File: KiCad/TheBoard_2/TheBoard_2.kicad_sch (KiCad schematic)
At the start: 9 parts, among them J1 Conn_01x03_Female, J2 Conn_01x03_Female, J3 Conn_01x16_Female, J4 Conn_01x32_Male, J5 Conn_01x16_Female

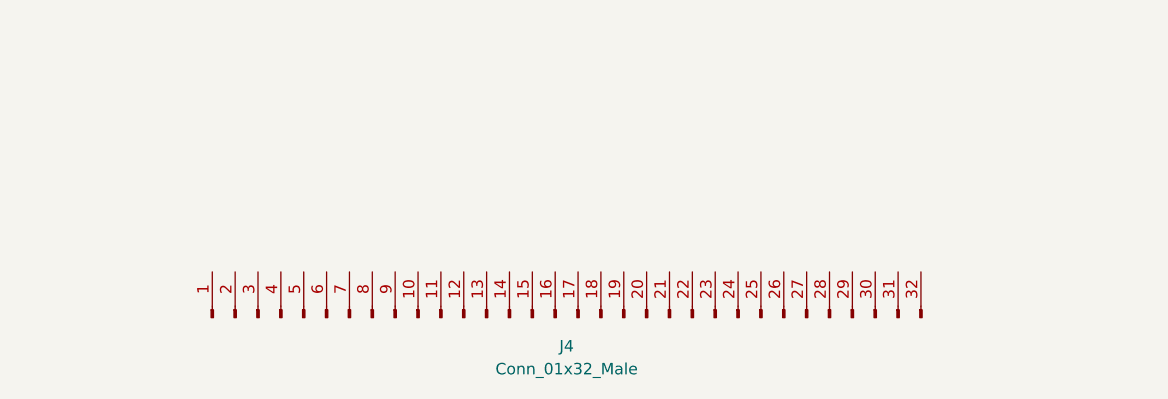
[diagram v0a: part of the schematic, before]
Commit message: Adding ground to output pins
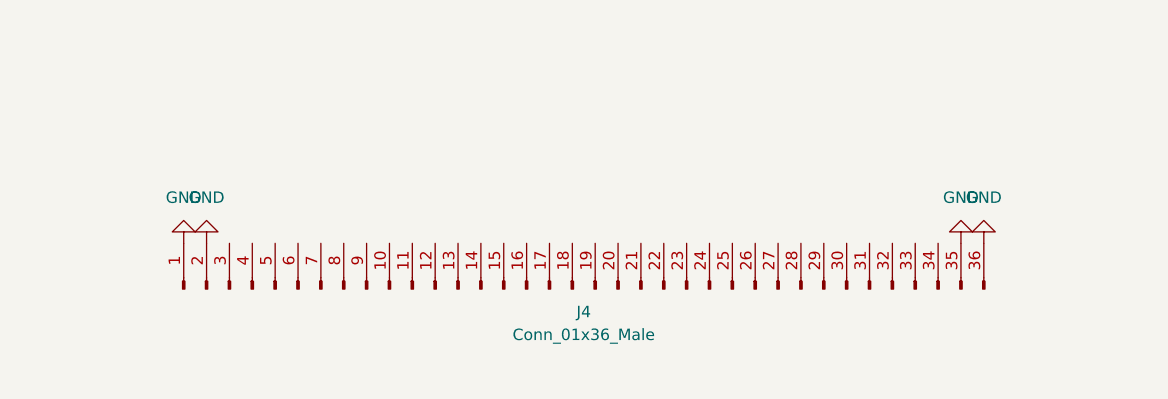
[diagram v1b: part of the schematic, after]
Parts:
- removed J4: Conn_01x32_Male, Connector_PinHeader_2.54mm:PinHeader_1x32_P2.54mm_Horizontal, symbol Connector:Conn_01x32_Male
- added J4: Conn_01x36_Male, Connector_PinHeader_2.54mm:PinHeader_2x18_P2.54mm_Horizontal, symbol Connector:Conn_01x36_Male
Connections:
- net GND: now also J4.1 (Pin_1), J4.2 (Pin_2), J4.35 (Pin_35), J4.36 (Pin_36)
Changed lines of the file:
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@@
     (pin "9")
   )
+  (symbol (lib_id "power:GND") (at 104.14 142.24 180) (unit 1)
+    (in_bom yes) (on_board yes) (fields_autoplaced)
+    (property "Reference" "#PWR0109" (id 0) (at 104.14 135.89 0)
+      (effects (font (size 1.27 1.27)) hide)
+    )
+    (property "Value" "GND" (id 1) (at 104.14 137.16 0))
+    (property "Footprint" "" (id 2) (at 104.14 142.24 0)
+      (effects (font (size 1.27 1.27)) hide)
+    )
+    (property "Datasheet" "" (id 3) (at 104.14 142.24 0)
+      (effects (font (size 1.27 1.27)) hide)
+    )
+    (pin "1")
+  )
   (symbol (lib_id "Mechanical:MountingHole") (at 36.195 30.48 0) (unit 1)
     (in_bom yes) (on_board yes) (fields_autoplaced)
@@
     )
   )
-  (symbol (lib_id "Mechanical:MountingHole") (at 36.195 20.32 0) (unit 1)
-    (in_bom yes) (on_board yes) (fields_autoplaced)
-    (property "Reference" "H2" (id 0) (at 38.735 19.0499 0)
-      (effects (font (size 1.27 1.27)) (justify left))
-    )
-    (property "Value" "MountingHole" (id 1) (at 38.735 21.5899 0)
-      (effects (font (size 1.27 1.27)) (justify left))
-    )
-    (property "Footprint" "MountingHole:MountingHole_3mm" (id 2) (at 36.195 20.32 0)
-      (effects (font (size 1.27 1.27)) hide)
-    )
-    (property "Datasheet" "~" (id 3) (at 36.195 20.32 0)
-      (effects (font (size 1.27 1.27)) hide)
-    )
-  )
-  (symbol (lib_id "Connector:Conn_01x32_Male") (at 145.415 150.495 90) (unit 1)
-    (in_bom yes) (on_board yes) (fields_autoplaced)
-    (property "Reference" "J4" (id 0) (at 146.685 153.67 90))
-    (property "Value" "Conn_01x32_Male" (id 1) (at 146.685 156.21 90))
-    (property "Footprint" "Connector_PinHeader_2.54mm:PinHeader_1x32_P2.54mm_Horizontal" (id 2) (at 145.415 150.495 0)
-      (effects (font (size 1.27 1.27)) hide)
-    )
-    (property "Datasheet" "~" (id 3) (at 145.415 150.495 0)
+  (symbol (lib_id "Connector:Conn_01x36_Male") (at 147.32 147.32 90) (unit 1)
+    (in_bom yes) (on_board yes) (fields_autoplaced)
+    (property "Reference" "J4" (id 0) (at 148.59 149.86 90))
+    (property "Value" "Conn_01x36_Male" (id 1) (at 148.59 152.4 90))
+    (property "Footprint" "Connector_PinHeader_2.54mm:PinHeader_2x18_P2.54mm_Horizontal" (id 2) (at 147.32 147.32 0)
+      (effects (font (size 1.27 1.27)) hide)
+    )
+    (property "Datasheet" "~" (id 3) (at 147.32 147.32 0)
       (effects (font (size 1.27 1.27)) hide)
     )
@@
     (pin "31")
     (pin "32")
+    (pin "33")
+    (pin "34")
+    (pin "35")
+    (pin "36")
     (pin "4")
     (pin "5")
@@
     (pin "8")
     (pin "9")
+  )
+  (symbol (lib_id "power:GND") (at 106.68 142.24 180) (unit 1)
+    (in_bom yes) (on_board yes) (fields_autoplaced)
+    (property "Reference" "#PWR0108" (id 0) (at 106.68 135.89 0)
+      (effects (font (size 1.27 1.27)) hide)
+    )
+    (property "Value" "GND" (id 1) (at 106.68 137.16 0))
+    (property "Footprint" "" (id 2) (at 106.68 142.24 0)
+      (effects (font (size 1.27 1.27)) hide)
+    )
+    (property "Datasheet" "" (id 3) (at 106.68 142.24 0)
+      (effects (font (size 1.27 1.27)) hide)
+    )
+    (pin "1")
+  )
+  (symbol (lib_id "Mechanical:MountingHole") (at 36.195 20.32 0) (unit 1)
+    (in_bom yes) (on_board yes) (fields_autoplaced)
+    (property "Reference" "H2" (id 0) (at 38.735 19.0499 0)
+      (effects (font (size 1.27 1.27)) (justify left))
+    )
+    (property "Value" "MountingHole" (id 1) (at 38.735 21.5899 0)
+      (effects (font (size 1.27 1.27)) (justify left))
+    )
+    (property "Footprint" "MountingHole:MountingHole_3mm" (id 2) (at 36.195 20.32 0)
+      (effects (font (size 1.27 1.27)) hide)
+    )
+    (property "Datasheet" "~" (id 3) (at 36.195 20.32 0)
+      (effects (font (size 1.27 1.27)) hide)
+    )
   )
   (symbol (lib_id "Connector:Conn_01x16_Female") (at 233.045 93.98 180) (unit 1)
@@
     (pin "9")
   )
+  (symbol (lib_id "power:GND") (at 193.04 142.24 180) (unit 1)
+    (in_bom yes) (on_board yes) (fields_autoplaced)
+    (property "Reference" "#PWR0107" (id 0) (at 193.04 135.89 0)
+      (effects (font (size 1.27 1.27)) hide)
+    )
+    (property "Value" "GND" (id 1) (at 193.04 137.16 0))
+    (property "Footprint" "" (id 2) (at 193.04 142.24 0)
+      (effects (font (size 1.27 1.27)) hide)
+    )
+    (property "Datasheet" "" (id 3) (at 193.04 142.24 0)
+      (effects (font (size 1.27 1.27)) hide)
+    )
+    (pin "1")
+  )
   (symbol (lib_id "power:GND") (at 38.735 46.99 90) (unit 1)
     (in_bom yes) (on_board yes) (fields_autoplaced)
@@
       (effects (font (size 1.27 1.27)) hide)
     )
+  )
+  (symbol (lib_id "power:GND") (at 190.5 142.24 180) (unit 1)
+    (in_bom yes) (on_board yes) (fields_autoplaced)
+    (property "Reference" "#PWR0110" (id 0) (at 190.5 135.89 0)
+      (effects (font (size 1.27 1.27)) hide)
+    )
+    (property "Value" "GND" (id 1) (at 190.5 137.16 0))
+    (property "Footprint" "" (id 2) (at 190.5 142.24 0)
+      (effects (font (size 1.27 1.27)) hide)
+    )
+    (property "Datasheet" "" (id 3) (at 190.5 142.24 0)
+      (effects (font (size 1.27 1.27)) hide)
+    )
+    (pin "1")
   )
   (symbol (lib_id "power:+5V") (at 38.735 40.005 270) (unit 1)
@@
       (reference "#PWR0106") (unit 1) (value "+5V") (footprint "")
     )
+    (path "/97874707-852c-4f97-b566-d5092c38fab4"
+      (reference "#PWR0107") (unit 1) (value "GND") (footprint "")
+    )
+    (path "/71a5fcca-2c92-4092-bc45-cdfd87fb70bf"
+      (reference "#PWR0108") (unit 1) (value "GND") (footprint "")
+    )
+    (path "/405b8a8b-22d1-47f5-a0bf-927117cf4560"
+      (reference "#PWR0109") (unit 1) (value "GND") (footprint "")
+    )
+    (path "/f1f5bd8f-cb69-40b6-8cd1-2d77afe2a46a"
+      (reference "#PWR0110") (unit 1) (value "GND") (footprint "")
+    )
     (path "/ebb6476c-0275-4763-a9ea-9c05ccdd35fd"
       (reference "H1") (unit 1) (value "MountingHole") (footprint "MountingHole:MountingHole_3mm")
@@
       (reference "J3") (unit 1) (value "Conn_01x16_Female") (footprint "Connector_PinHeader_2.54mm:PinHeader_1x16_P2.54mm_Vertical")
     )
-    (path "/7ea8b26d-d906-4bd8-95c7-418a065c7cd3"
-      (reference "J4") (unit 1) (value "Conn_01x32_Male") (footprint "Connector_PinHeader_2.54mm:PinHeader_1x32_P2.54mm_Horizontal")
+    (path "/6fa6f00b-82f4-4079-87ff-19d2eeb80891"
+      (reference "J4") (unit 1) (value "Conn_01x36_Male") (footprint "Connector_PinHeader_2.54mm:PinHeader_2x18_P2.54mm_Horizontal")
     )
     (path "/8e6013b4-e104-46a8-b12e-cbcbf0a129da"

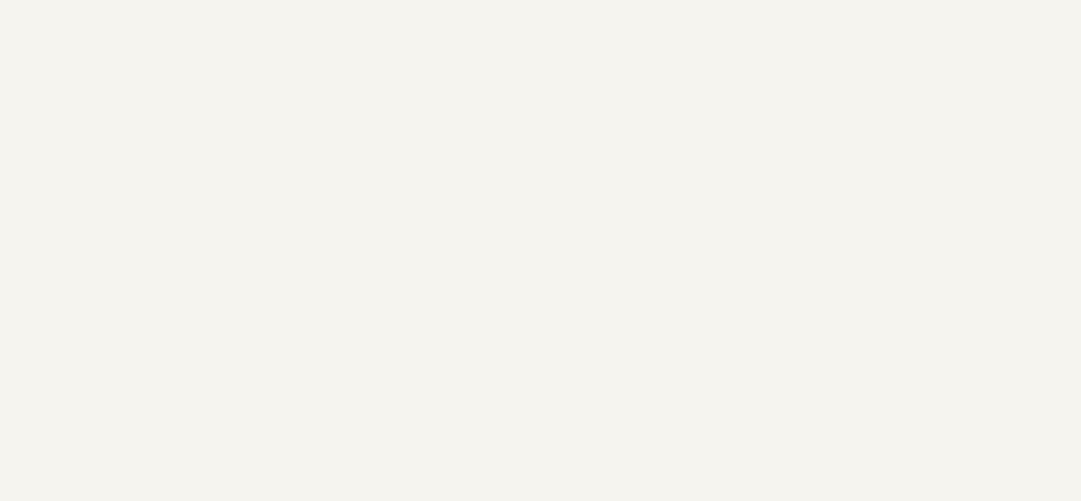
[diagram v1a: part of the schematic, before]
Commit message: Adding -5V circuit
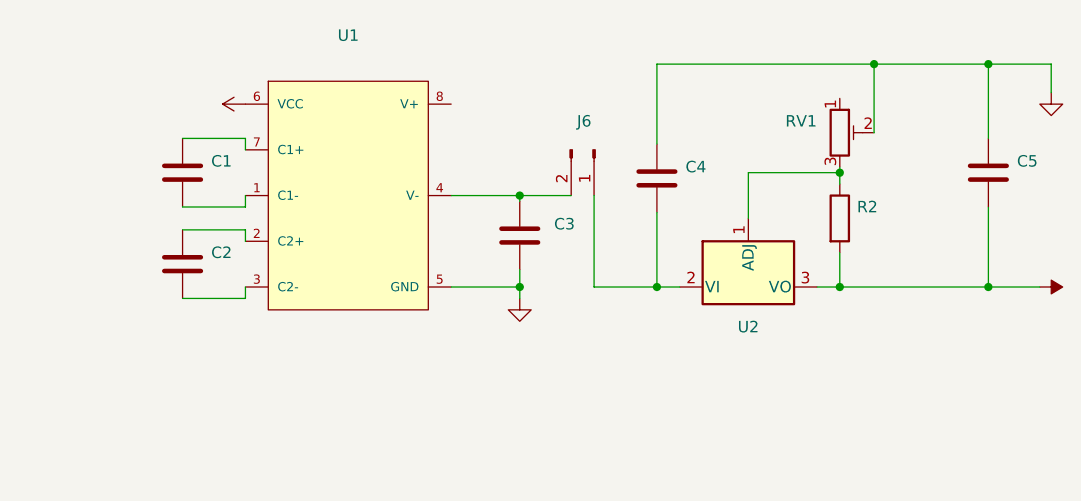
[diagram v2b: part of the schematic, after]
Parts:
- added C1, C2, C3, C4, C5: (no value), symbol Device:C
- added J6: (no value), symbol Connector:Conn_01x02_Male
- added R2: (no value), symbol Device:R
- added RV1: (no value), symbol Device:R_Potentiometer_Trim
- added U1: (no value), symbol eec:MAX680CSA+T
- added U2: (no value), symbol Regulator_Linear:LM337_TO220
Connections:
- net +5V: now also U1.6 (VCC)
- net GND: now also C3.2, C4.1, C5.1, RV1.2, U1.5 (GND)
- new net: R2.1, RV1.3, U2.1 (ADJ)
- new net: C4.2, J6.1 (Pin_1), U2.2 (VI)
- new net: C1.2, U1.1 (C1-)
- new net: C2.1, U1.2 (C2+)
- new net: C2.2, U1.3 (C2-)
- new net: C3.1, J6.2 (Pin_2), U1.4 (V-)
- new net: C1.1, U1.7 (C1+)
- new net -5V: C5.2, R2.2, U2.3 (VO)

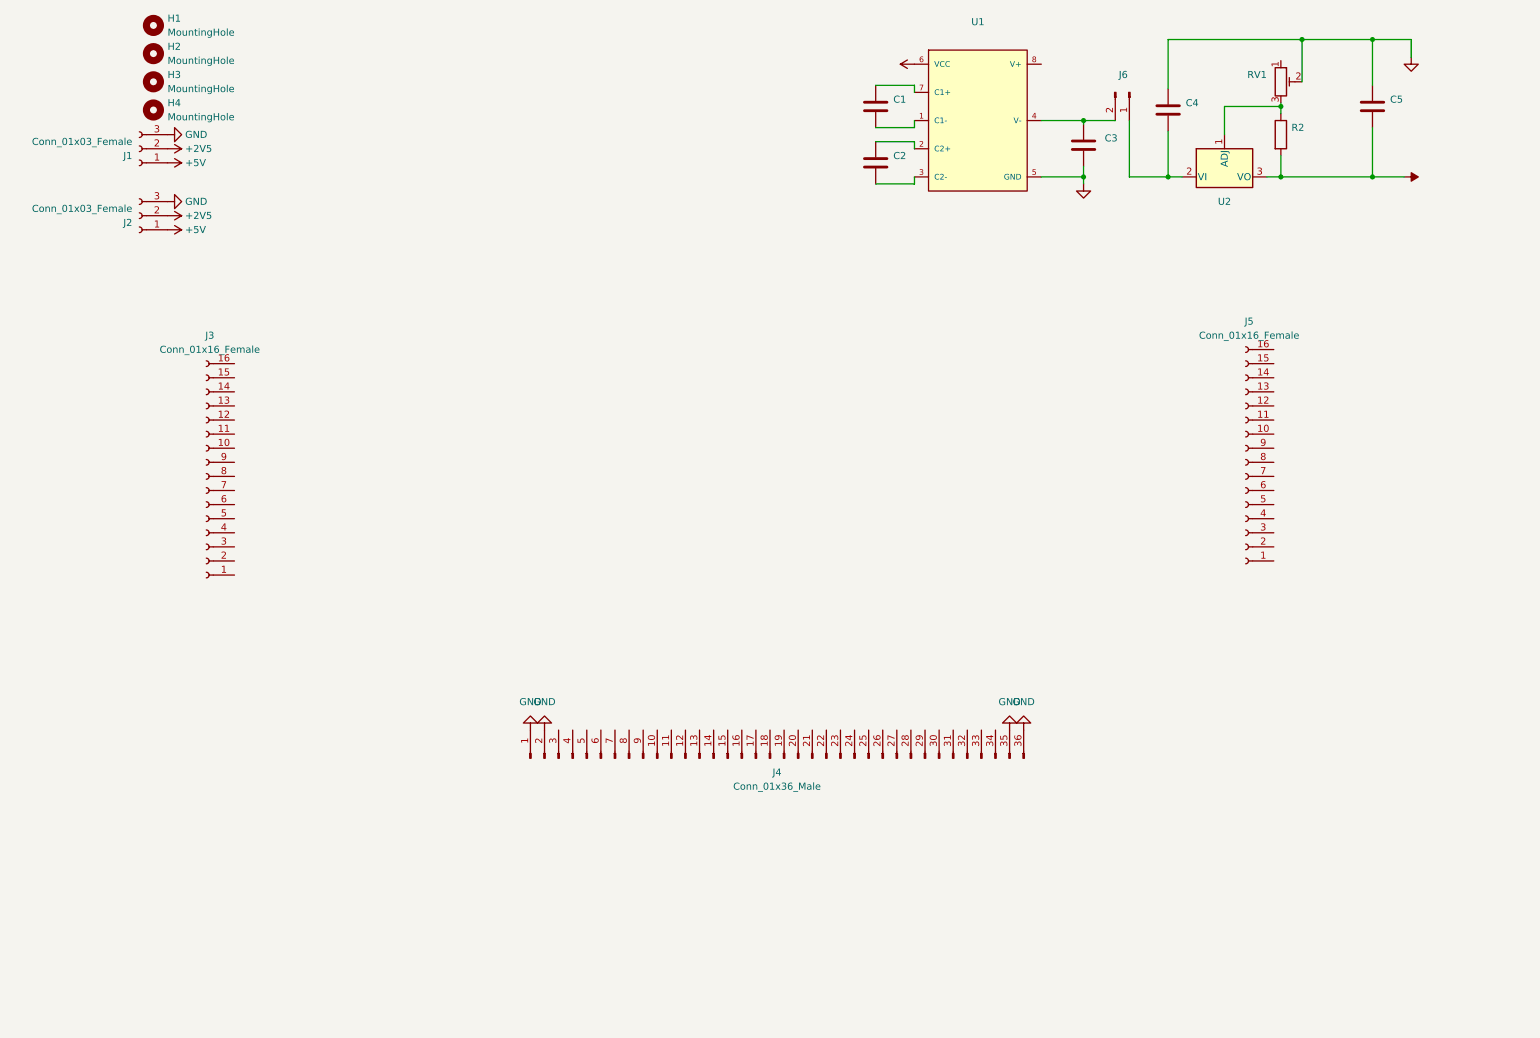
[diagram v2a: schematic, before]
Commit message: adding mt3608 circuit
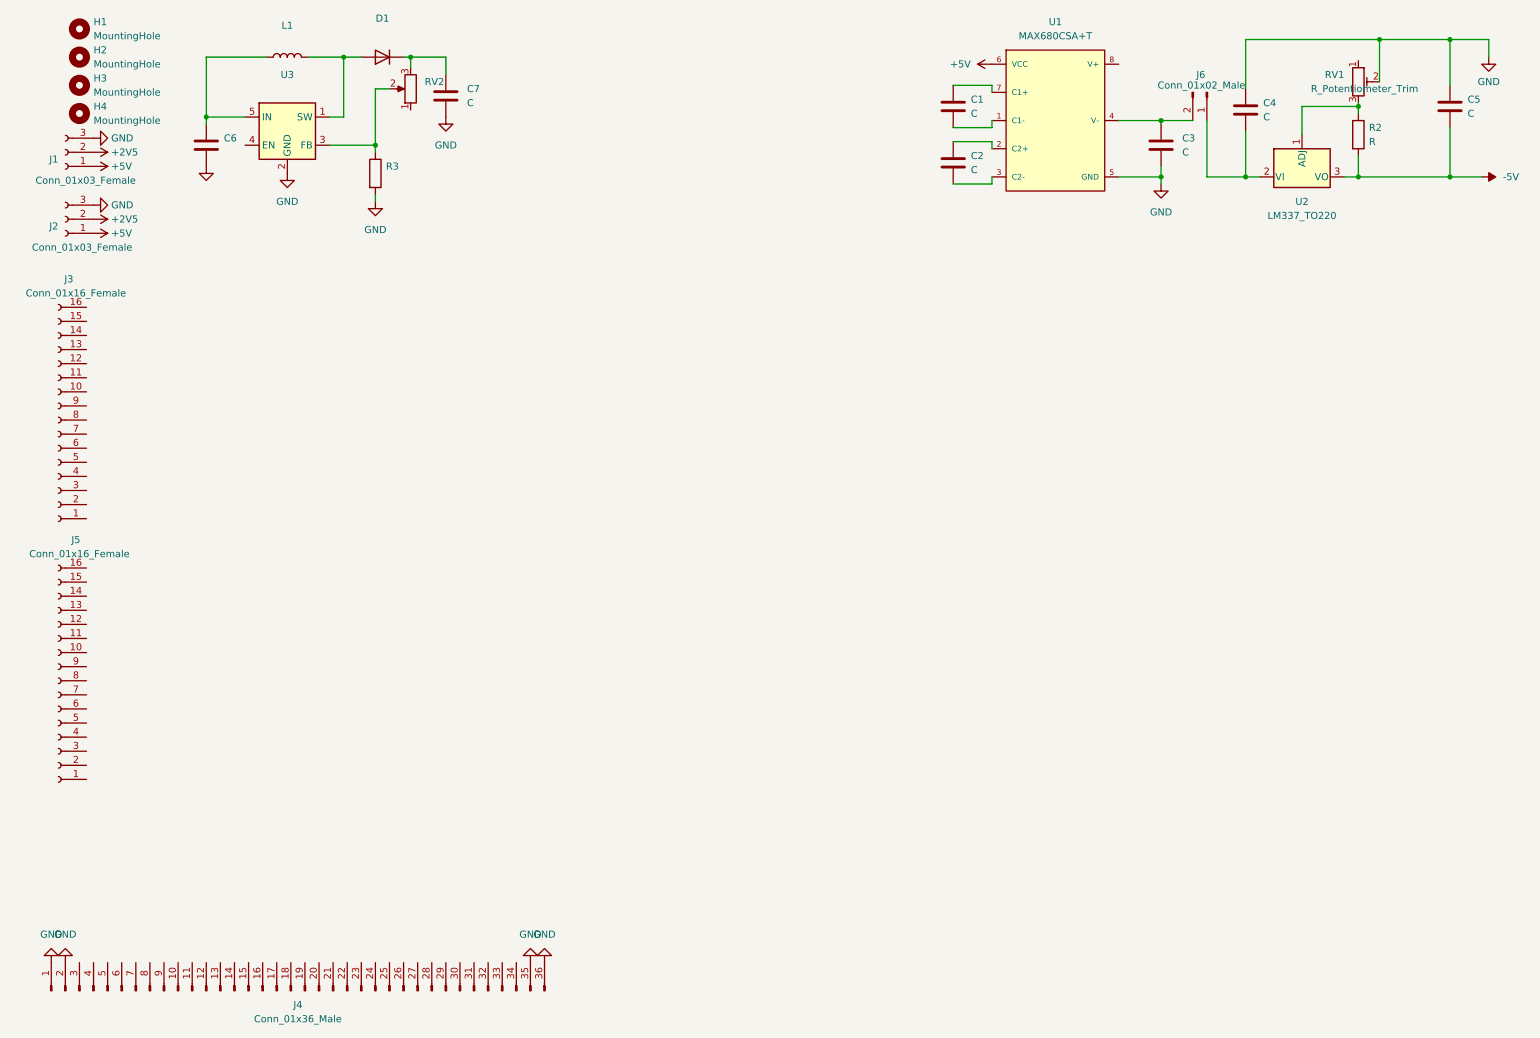
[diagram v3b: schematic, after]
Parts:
- added C6: (no value), symbol Device:C
- added C7: C, symbol Device:C
- added D1: (no value), symbol Device:D
- added L1: (no value), symbol Device:L
- added R3: (no value), symbol Device:R
- added RV2: (no value), symbol Device:R_Potentiometer
- added U3: (no value), symbol Regulator_Switching:MT3608
- C1, C2, C3, C4, C5: value (none) -> C; footprint (none) -> Capacitor_THT:CP_Radial_D8.0mm_P5.00mm
- J6: value (none) -> Conn_01x02_Male; footprint (none) -> Connector_PinHeader_2.54mm:PinHeader_1x02_P2.54mm_Vertical
- R2: value (none) -> R; footprint (none) -> Resistor_THT:R_Axial_DIN0207_L6.3mm_D2.5mm_P7.62mm_Horizontal
- RV1: value (none) -> R_Potentiometer_Trim; footprint (none) -> Potentiometer_THT:Potentiometer_Bourns_3296W_Vertical
- U1: value (none) -> MAX680CSA+T; footprint (none) -> Package_DIP:DIP-8_W7.62mm_LongPads
- U2: value (none) -> LM337_TO220; footprint (none) -> Package_TO_SOT_THT:TO-220-3_Vertical
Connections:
- net GND: now also C6.2, C7.2, R3.2, U3.2 (GND)
- new net: D1.2 (A), L1.2, U3.1 (SW)
- new net: R3.1, RV2.2, U3.3 (FB)
- new net: C6.1, L1.1, U3.5 (IN)
- new net: C7.1, D1.1 (K), RV2.3
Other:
- moved on the sheet: C1, C2, C3, C4, C5, H1, H2, H3, H4, J1, J2, J3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

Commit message: Adding battery circuit
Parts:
- added C10, C9: C, symbol Device:C
- added C8: (no value), symbol Device:C
- added D2: (no value), symbol Device:LED
- added D3: LED, symbol Device:LED
- added J7: (no value), symbol Connector:USB_B_Micro
- added Q1: (no value), symbol FS8205A:FS8205A
- added R1: (no value), symbol Device:R
- added R4, R5, R6, R7: R, symbol Device:R
- added U4: TP4056, Package_SO:SOIC-8-1EP_3.9x4.9mm_P1.27mm_EP2.29x3mm, symbol tp4056:TP4056
- added U5: DW01, Package_TO_SOT_SMD:SOT-23-6_Handsoldering, symbol dw01:DW01
- C6: value (none) -> C; footprint (none) -> Capacitor_SMD:C_1206_3216Metric
- C7: footprint (none) -> Capacitor_SMD:C_1206_3216Metric
- D1: value (none) -> D; footprint (none) -> Diode_SMD:D_SMA
- L1: value (none) -> L; footprint (none) -> Inductor_SMD:L_10.4x10.4_H4.8
- R3: value (none) -> R; footprint (none) -> Resistor_SMD:R_0805_2012Metric
- RV2: value (none) -> R_Potentiometer; footprint (none) -> Potentiometer_THT:Potentiometer_Bourns_3296P_Horizontal
- U3: value (none) -> MT3608; footprint (none) -> Package_TO_SOT_SMD:SOT-23-6
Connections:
- net GND: now also C10.2, C8.2, J7.5 (GND), Q1.6, Q1.7, R5.2, R6.2, U4.1 (TEMP), U4.3 (GND)
- new net: C8.1, D2.2 (A), D3.2 (A), J7.1 (VBUS), U4.4 (VCC), U4.8 (CE)
- new net: Q1.4, U5.1 (OD)
- new net: R6.1, U5.2 (CS)
- new net: Q1.5, U5.3 (OC)
- new net: C9.1, R7.1, U5.5 (VCC)
- new net: D2.1 (K), R1.1
- new net: Q1.1, Q1.8
- new net: D3.1 (K), R4.1
- new net: R5.1, U4.2 (PROG)
- new net: R4.2, U4.6 (~{STDBY})
- new net: R1.2, U4.7 (~{CHRG})
- new net B-: C9.2, Q1.2, Q1.3, U5.6 (GND)
- new net OUT/B+: C10.1, R7.2, U4.5 (BAT)
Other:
- moved on the sheet: C1, C2, C3, C4, C5, C6, C7, D1, J6, L1, R2, R3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
